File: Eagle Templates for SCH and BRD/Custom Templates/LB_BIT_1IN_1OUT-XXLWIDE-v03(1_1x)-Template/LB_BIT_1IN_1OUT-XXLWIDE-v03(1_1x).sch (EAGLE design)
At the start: 16 parts, among them U1 LV321SOT23-5, U2 LV321SOT23-5

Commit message: added bitlab logo and made minor changes to board templates. Updated littlebits library.
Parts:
- renumbered FRAME1 to U$3
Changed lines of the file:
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@@
 <layer number="111" name="LB_TEXT" color="13" fill="1" visible="yes" active="yes"/>
 <layer number="112" name="tSilk" color="7" fill="1" visible="yes" active="yes"/>
+<layer number="113" name="ReferenceLS" color="7" fill="1" visible="no" active="yes"/>
 <layer number="116" name="Patch_BOT" color="9" fill="4" visible="yes" active="yes"/>
+<layer number="118" name="Rect_Pads" color="7" fill="1" visible="no" active="yes"/>
 <layer number="121" name="_tsilk" color="7" fill="1" visible="yes" active="yes"/>
 <layer number="122" name="_bsilk" color="7" fill="1" visible="yes" active="yes"/>
@@
 <attribute name="VOLTAGE" value=""/>
 </part>
-<part name="FRAME1" library="LITTLEBITS" deviceset="FRAME-LETTER" device=""/>
+<part name="U$3" library="LITTLEBITS" deviceset="FRAME-LETTER" device=""/>
 </parts>
 <sheets>
@@
 <attribute name="VALUE" x="125.984" y="142.621" size="1.778" layer="96"/>
 </instance>
-<instance part="FRAME1" gate="G$1" x="0" y="0"/>
-<instance part="FRAME1" gate="G$2" x="147.32" y="0"/>
+<instance part="U$3" gate="G$1" x="0" y="0"/>
+<instance part="U$3" gate="G$2" x="147.32" y="0"/>
 </instances>
 <busses>

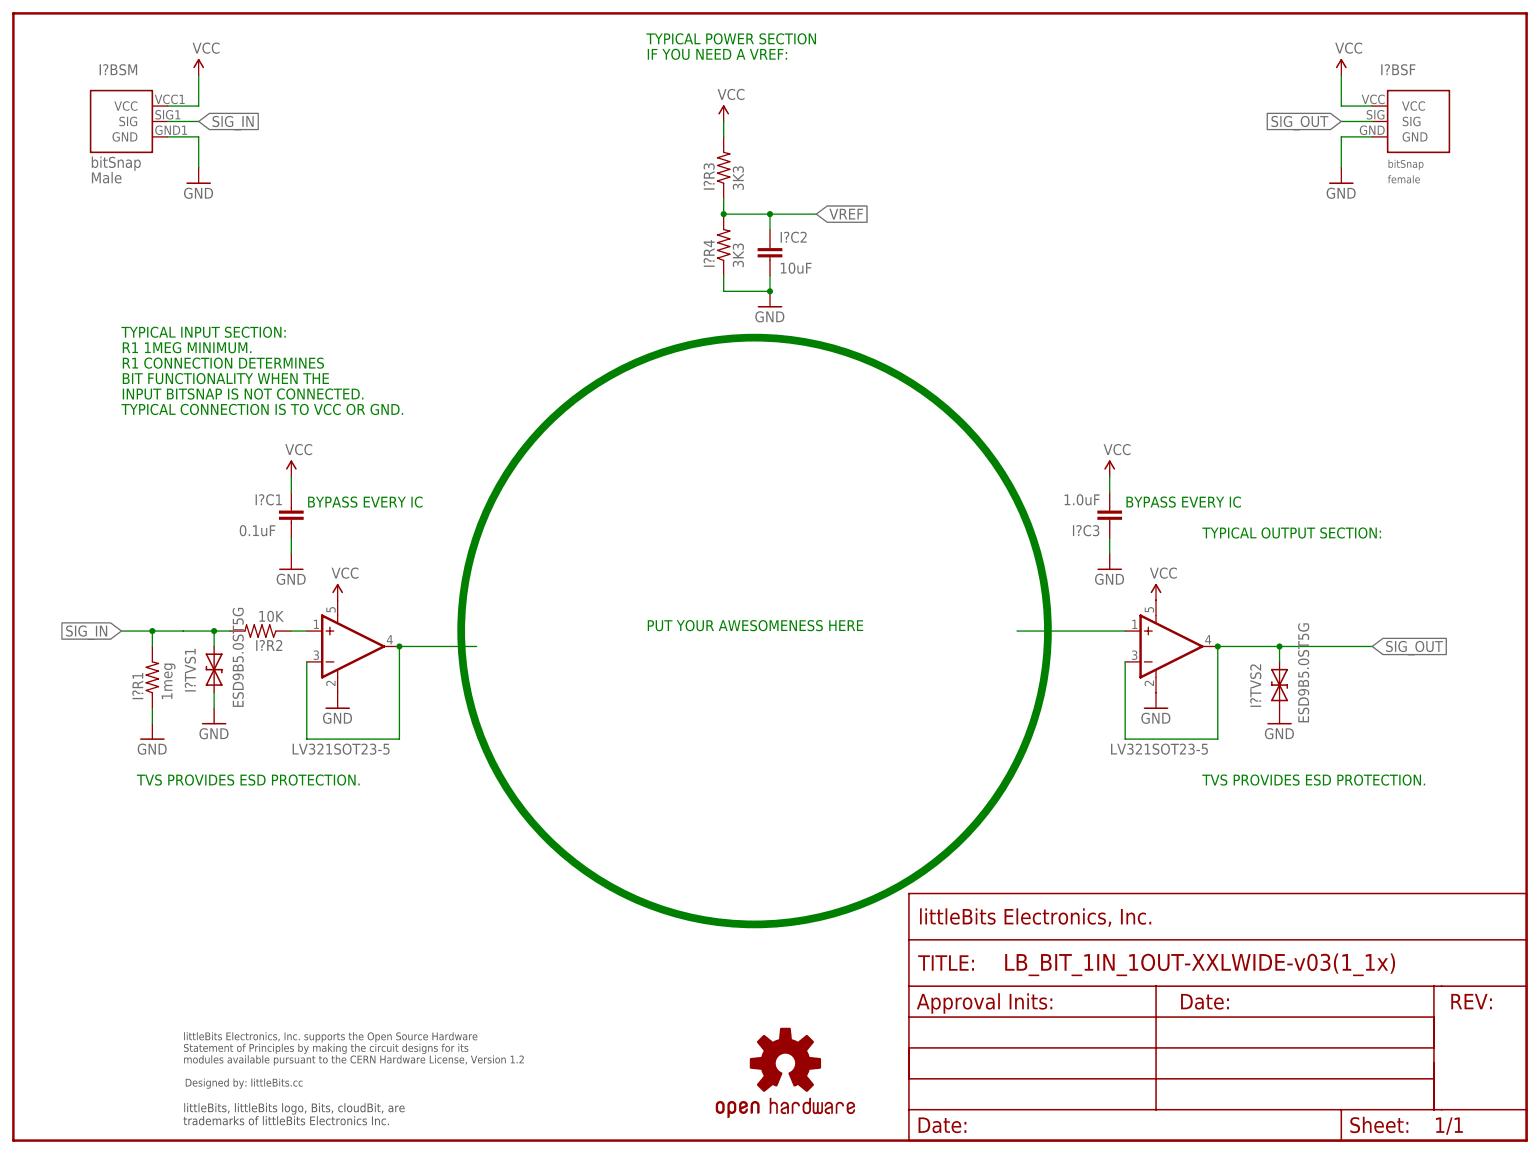
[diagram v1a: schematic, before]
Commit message: Updated templates
- Added ferrite beads
- Moved text and annotations off of Nets layer
- Minor layout changes
- Removed I/O/W prefix from reference designators
- Removed output stage components from output bits
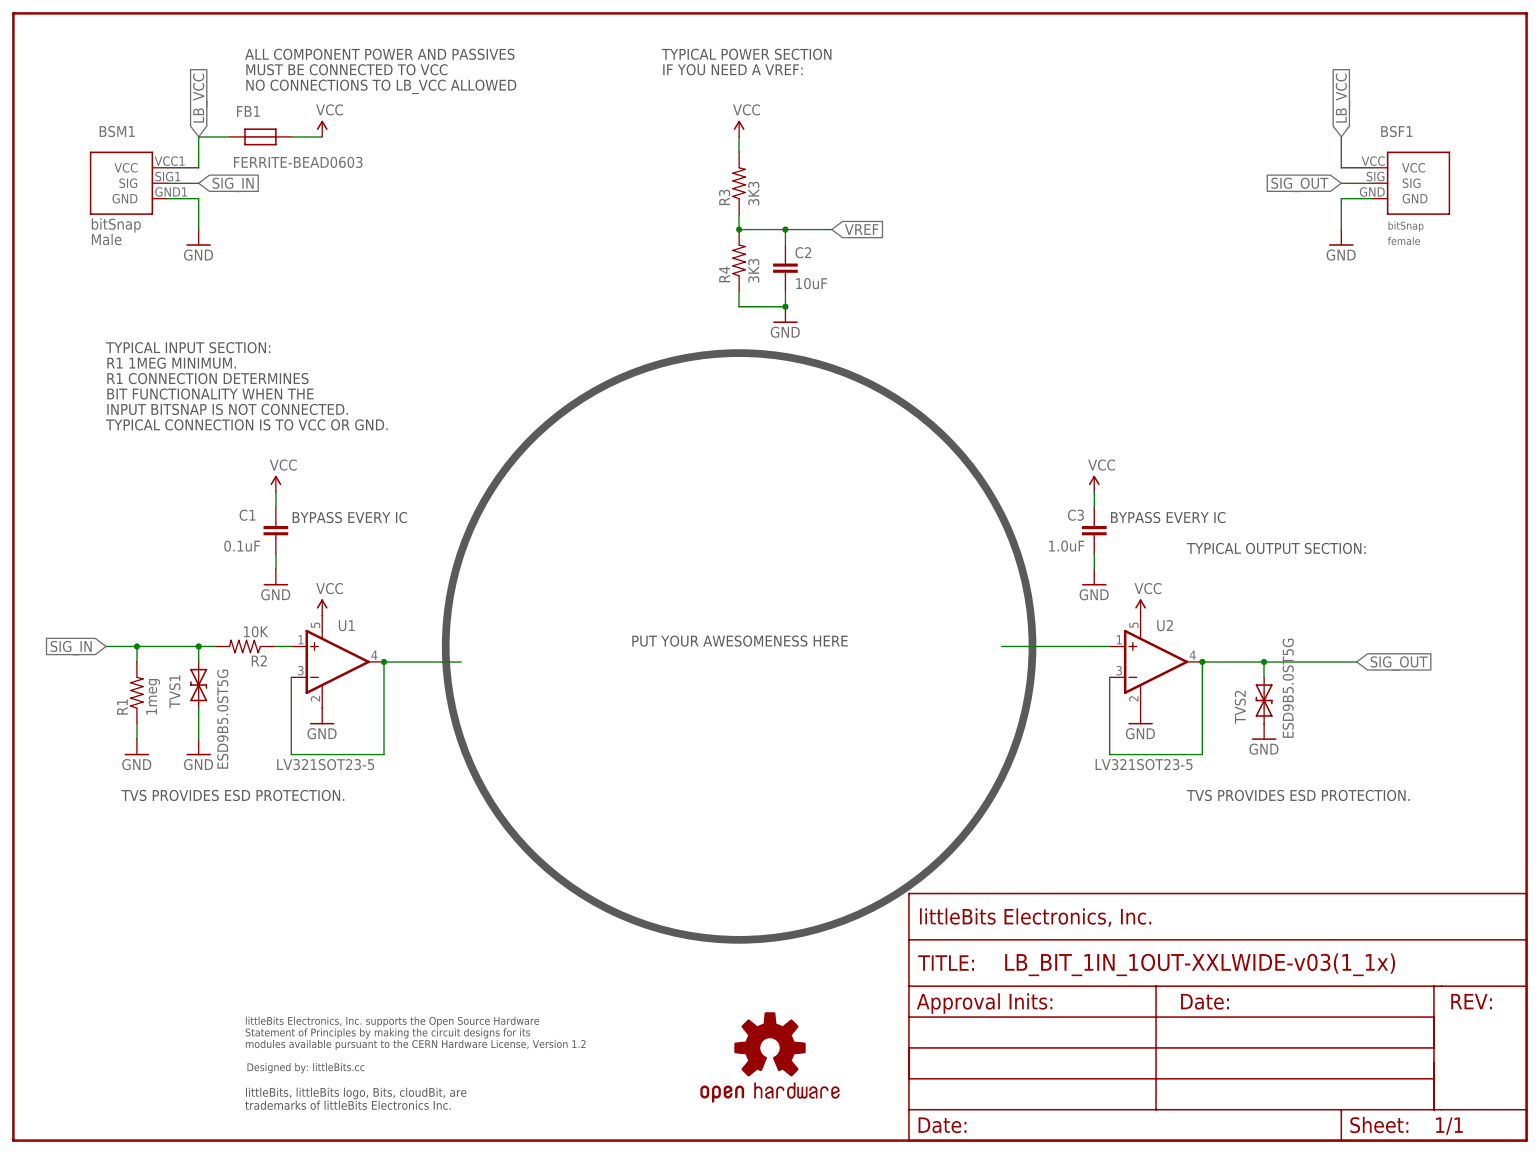
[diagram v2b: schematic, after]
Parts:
- removed I?BSF: BITSNAP_V03_FEMALE, bitSnap:BITSNAP_V03_FEMALE
- removed I?BSM: BITSNAP_V03_MALE, bitSnap:BITSNAP_V03_MALE
- removed I?C1: 0.1uF, LITTLEBITS:CAPCAP-0603
- removed I?C2: 10uF, LITTLEBITS:CAPCAP-0603
- removed I?C3: 1.0uF, LITTLEBITS:CAPCAP-0603
- removed I?R1: 1meg, LITTLEBITS:RESISTOR0603
- removed I?R2: 10K, LITTLEBITS:RESISTOR0603
- removed I?R3, I?R4: 3K3, LITTLEBITS:RESISTOR0603
- removed I?TVS1, I?TVS2: ESD9B5.0ST5G, LITTLEBITS:DIODE-TVSSOD-923
- removed U$3: FRAME-LETTER, LITTLEBITS:FRAME-LETTER
- added BSF1: BITSNAP_V03_FEMALE, bitSnap:BITSNAP_V03_FEMALE
- added BSM1: BITSNAP_V03_MALE, bitSnap:BITSNAP_V03_MALE
- added C1: 0.1uF, LITTLEBITS:CAPCAP-0603
- added C2: 10uF, LITTLEBITS:CAPCAP-0603
- added C3: 1.0uF, LITTLEBITS:CAPCAP-0603
- added FB1: FERRITE-BEAD0603, LITTLEBITS:FERRITE-BEAD0603
- added R1: 1meg, LITTLEBITS:RESISTOR0603
- added R2: 10K, LITTLEBITS:RESISTOR0603
- added R3, R4: 3K3, LITTLEBITS:RESISTOR0603
- added TVS1, TVS2: ESD9B5.0ST5G, LITTLEBITS:DIODE-TVSSOD-923
- added U$5: FRAME-LETTER-OHWOHW, LITTLEBITS:FRAME-LETTER-OHWOHW
- U$1: value OSHWCREDIT -> OSHW-LOGOL; device LITTLEBITS:OSHWCREDIT -> LITTLEBITS131206:OSHW-LOGOL
- U$2: value OSHW-LOGOL -> OSHWCREDIT; device LITTLEBITS131206:OSHW-LOGOL -> LITTLEBITS:OSHWCREDIT
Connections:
- removed net N$9: I?R2.1, U1.+IN
- new net LB_VCC: BSF1.VCC, BSM1.VCC, FB1.P$2
- new net N$4: R2.1, U1.+IN
- net GND: now also BSF1.GND, BSM1.GND, C1.2, C2.2, C3.1, R1.1, R4.1, TVS1.A, TVS2.A; no longer I?BSF.GND, I?BSM.GND, I?C1.2, I?C2.2, I?C3.1, I?R1.1, I?R4.1, I?TVS1.A, I?TVS2.A
- net SIG_IN: now also BSM1.SIG, R1.2, R2.2, TVS1.C; no longer I?BSM.SIG, I?R1.2, I?R2.2, I?TVS1.C
- net SIG_OUT: now also BSF1.SIG, TVS2.C; no longer I?BSF.SIG, I?TVS2.C
- net VCC: now also C1.1, C3.2, FB1.P$1, R3.2; no longer I?BSF.VCC, I?BSM.VCC, I?C1.1, I?C3.2, I?R3.2
- net VREF: now also C2.1, R3.1, R4.2; no longer I?C2.1, I?R3.1, I?R4.2
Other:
- note added: "ALL COMPONENT POWER AND PASSIVES"
- note added: "MUST BE CONNECTED TO VCC"
- note added: "NO CONNECTIONS TO LB_VCC ALLOWED"
